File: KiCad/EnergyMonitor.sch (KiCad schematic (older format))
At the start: 28 parts

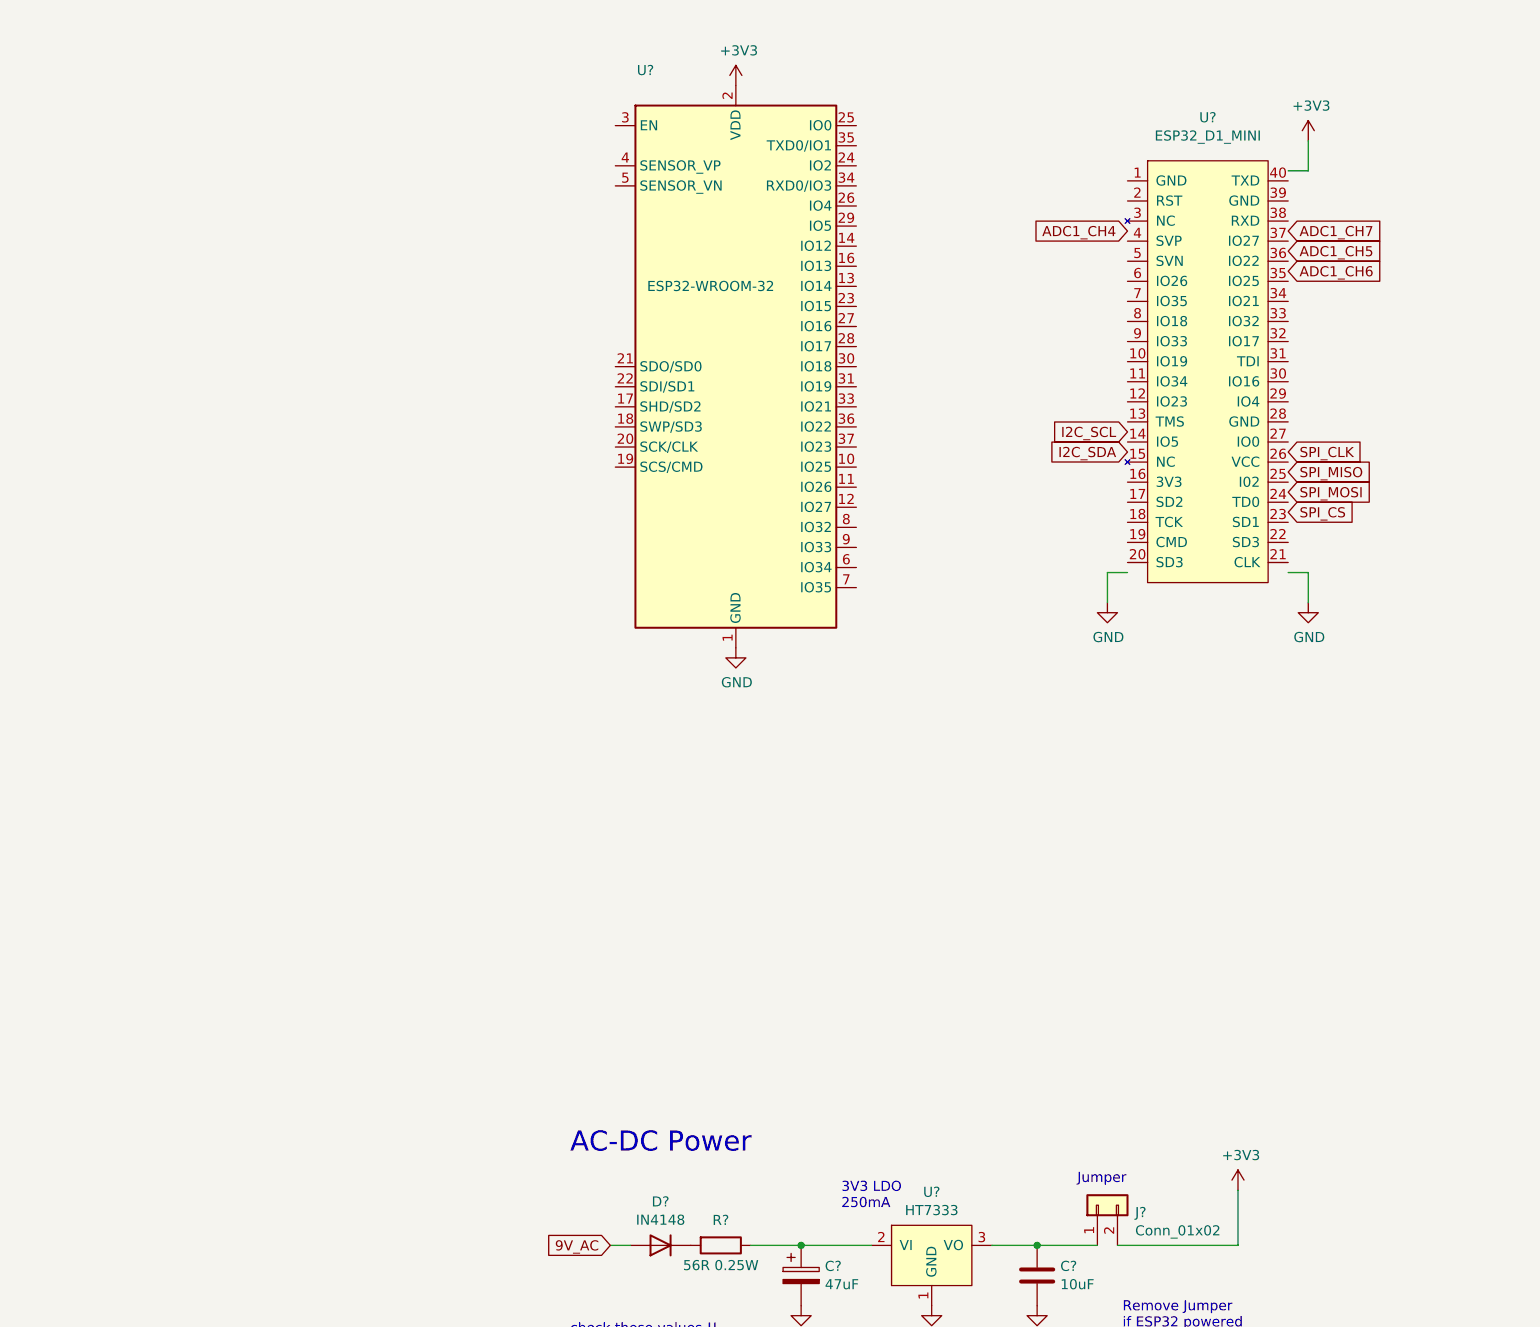
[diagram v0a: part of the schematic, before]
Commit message: edit ESP32_D1_MINI Symbol
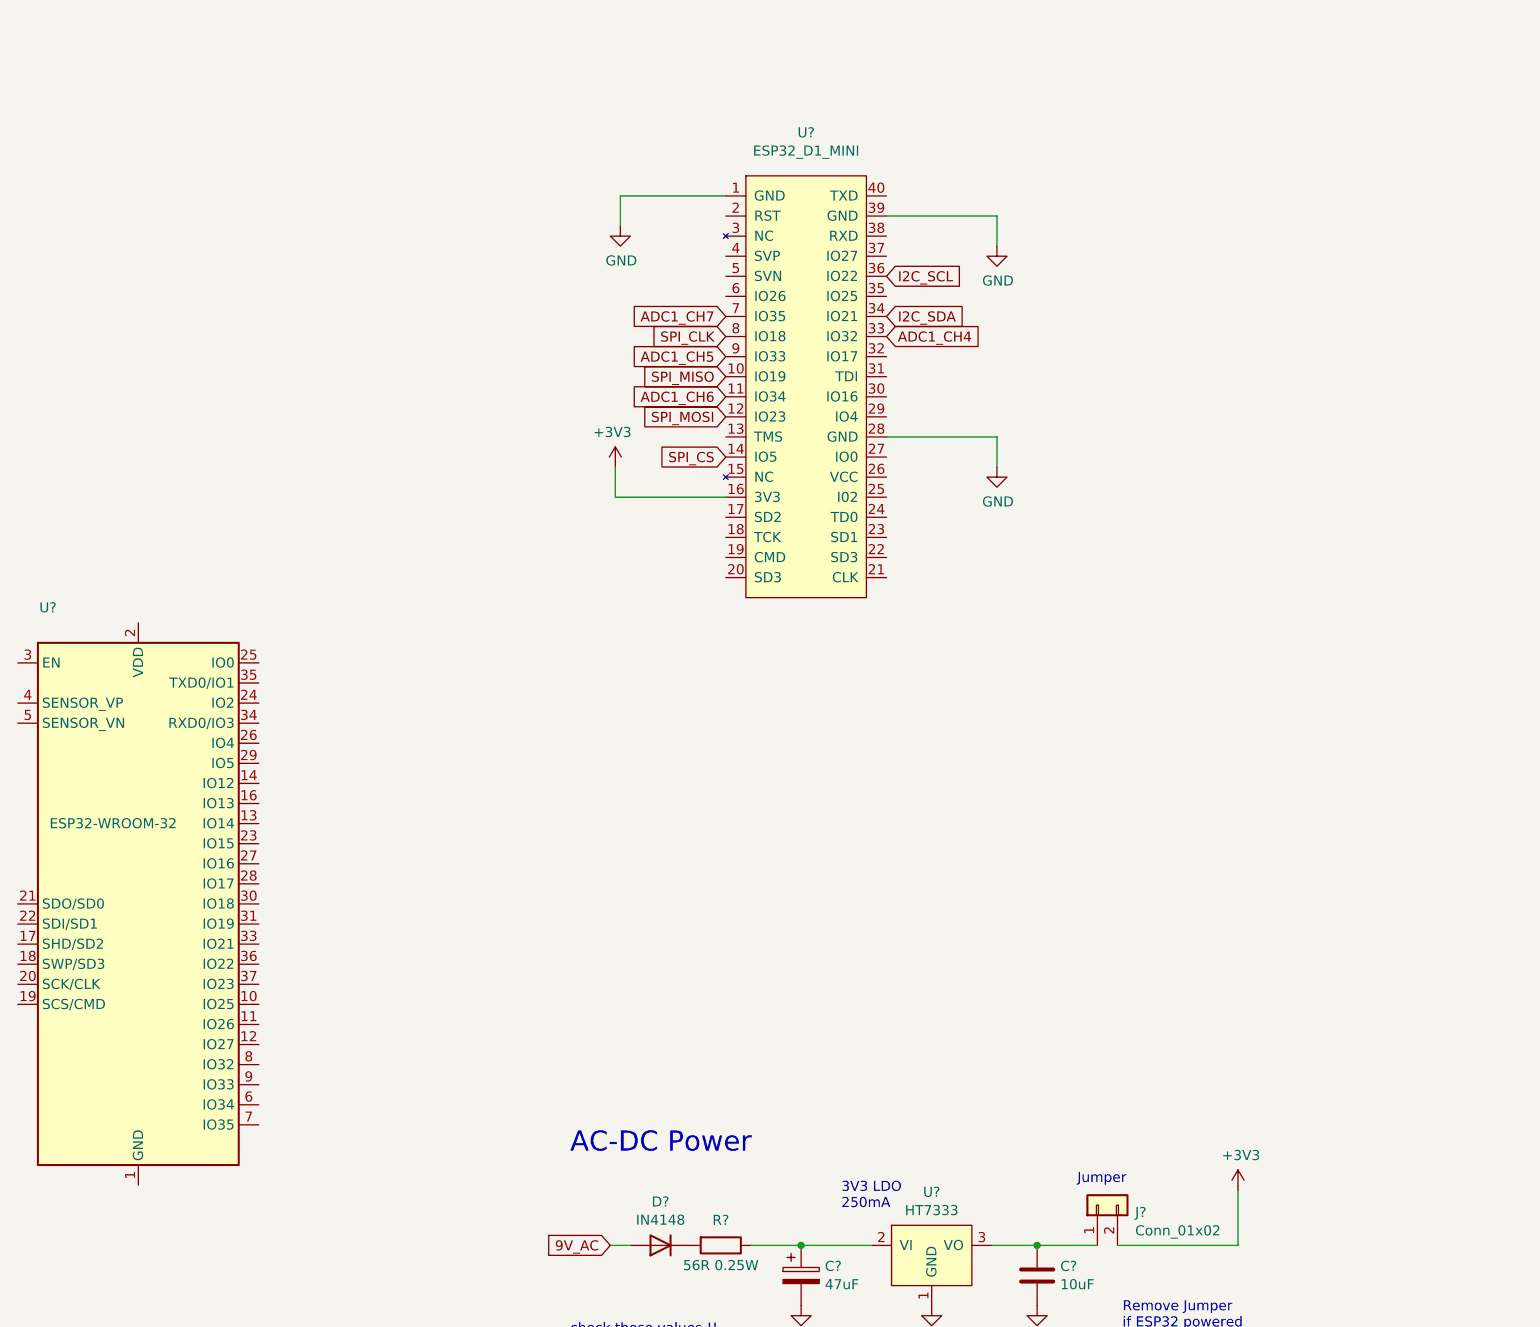
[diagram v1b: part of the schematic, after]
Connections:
- wire segments 52 -> 54
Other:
- moved on the sheet: U?
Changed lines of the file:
@@
 Sheet 1 1
 Title "ESP32 Energy Monitor"
-Date "2021-09-04"
+Date "2021-09-05"
 Rev "v1.0"
 Comp ""
@@
 Comment4 "klomar"
 $EndDescr
-Text GLabel 4450 2100 2    50   Input ~ 0
+Text GLabel 1650 2725 0    50   Input ~ 0
 ADC1_CH6
-Text GLabel 4450 1900 2    50   Input ~ 0
+Text GLabel 1650 2325 0    50   Input ~ 0
 ADC1_CH7
 $Comp
 L power:GND #PWR?
-U 1 1 6131BED5
-P 1700 3975
-F 0 "#PWR?" H 1700 3725 50  0001 C CNN
-F 1 "GND" H 1705 3802 50  0000 C CNN
-F 2 "" H 1700 3975 50  0001 C CNN
-F 3 "" H 1700 3975 50  0001 C CNN
-	1    1700 3975
-	1    0    0    -1
-$EndComp
-$Comp
-L power:+3V3 #PWR?
-U 1 1 6131CC87
-P 1700 1175
-F 0 "#PWR?" H 1700 1025 50  0001 C CNN
-F 1 "+3V3" H 1715 1348 50  0000 C CNN
-F 2 "" H 1700 1175 50  0001 C CNN
-F 3 "" H 1700 1175 50  0001 C CNN
-	1    1700 1175
-	1    0    0    -1
-$EndComp
-$Comp
-L power:GND #PWR?
 U 1 1 6135620D
 P 10225 3050
@@
 L RF_Module:ESP32-WROOM-32 U?
 U 1 1 613185A1
-P 1700 2575
-F 0 "U?" H 1250 4050 50  0000 C CNN
-F 1 "ESP32-WROOM-32" H 1575 2975 50  0000 C CNN
-F 2 "RF_Module:ESP32-WROOM-32" H 1700 1075 50  0001 C CNN
-F 3 "https://www.espressif.com/sites/default/files/documentation/esp32-wroom-32_datasheet_en.pdf" H 1400 2625 50  0001 C CNN
-	1    1700 2575
+P -1275 5250
+F 0 "U?" H -1725 6725 50  0000 C CNN
+F 1 "ESP32-WROOM-32" H -1400 5650 50  0000 C CNN
+F 2 "RF_Module:ESP32-WROOM-32" H -1275 3750 50  0001 C CNN
+F 3 "https://www.espressif.com/sites/default/files/documentation/esp32-wroom-32_datasheet_en.pdf" H -1575 5300 50  0001 C CNN
+	1    -1275 5250
 	1    0    0    -1
 $EndComp
@@
 Text Notes 3625 7450 0    50   ~ 0
 Remove Jumper\nif ESP32 powered\nby USB.
-Text GLabel 4450 2000 2    50   Input ~ 0
+Text GLabel 1650 2525 0    50   Input ~ 0
 ADC1_CH5
-Text GLabel 3650 1900 0    50   Input ~ 0
+Text GLabel 2450 2425 2    50   Input ~ 0
 ADC1_CH4
-Text GLabel 3650 2900 0    50   Input ~ 0
+Text GLabel 2450 2125 2    50   Input ~ 0
 I2C_SCL
-Text GLabel 3650 3000 0    50   Input ~ 0
+Text GLabel 2450 2325 2    50   Input ~ 0
 I2C_SDA
-Text GLabel 4450 3200 2    50   Input ~ 0
+Text GLabel 1650 2825 0    50   Input ~ 0
 SPI_MOSI
-Text GLabel 4450 3100 2    50   Input ~ 0
+Text GLabel 1650 2625 0    50   Input ~ 0
 SPI_MISO
-Text GLabel 4450 3000 2    50   Input ~ 0
+Text GLabel 1650 2425 0    50   Input ~ 0
 SPI_CLK
-Text GLabel 4450 3300 2    50   Input ~ 0
+Text GLabel 1650 3025 0    50   Input ~ 0
 SPI_CS
 Text GLabel 10475 1100 2    50   Input ~ 0
@@
 L MyComponents:ESP32_D1_MINI U?
 U 1 1 6133B216
-P 4050 2600
-F 0 "U?" H 4050 3865 50  0000 C CNN
-F 1 "ESP32_D1_MINI" H 4050 3774 50  0000 C CNN
-F 2 "" H 4050 3050 50  0001 C CNN
-F 3 "" H 4050 3050 50  0001 C CNN
-	1    4050 2600
+P 2050 2675
+F 0 "U?" H 2050 3940 50  0000 C CNN
+F 1 "ESP32_D1_MINI" H 2050 3849 50  0000 C CNN
+F 2 "" H 2050 3125 50  0001 C CNN
+F 3 "" H 2050 3125 50  0001 C CNN
+	1    2050 2675
 	1    0    0    -1
 $EndComp
@@
 L power:GND #PWR?
 U 1 1 613461CB
-P 3550 3750
-F 0 "#PWR?" H 3550 3500 50  0001 C CNN
-F 1 "GND" H 3555 3577 50  0000 C CNN
-F 2 "" H 3550 3750 50  0001 C CNN
-F 3 "" H 3550 3750 50  0001 C CNN
-	1    3550 3750
+P 1125 1875
+F 0 "#PWR?" H 1125 1625 50  0001 C CNN
+F 1 "GND" H 1130 1702 50  0000 C CNN
+F 2 "" H 1125 1875 50  0001 C CNN
+F 3 "" H 1125 1875 50  0001 C CNN
+	1    1125 1875
 	1    0    0    -1
 $EndComp
@@
 L power:GND #PWR?
 U 1 1 61346C95
-P 4550 3750
-F 0 "#PWR?" H 4550 3500 50  0001 C CNN
-F 1 "GND" H 4555 3577 50  0000 C CNN
-F 2 "" H 4550 3750 50  0001 C CNN
-F 3 "" H 4550 3750 50  0001 C CNN
-	1    4550 3750
+P 3000 1975
+F 0 "#PWR?" H 3000 1725 50  0001 C CNN
+F 1 "GND" H 3005 1802 50  0000 C CNN
+F 2 "" H 3000 1975 50  0001 C CNN
+F 3 "" H 3000 1975 50  0001 C CNN
+	1    3000 1975
 	1    0    0    -1
 $EndComp
 Wire Wire Line
-	4450 3600 4550 3600
+	2450 1825 3000 1825
 Wire Wire Line
-	4550 3600 4550 3750
+	3000 1825 3000 1975
 Wire Wire Line
-	3650 3600 3550 3600
+	1650 1725 1125 1725
 Wire Wire Line
-	3550 3600 3550 3750
+	1125 1725 1125 1875
 $Comp
 L power:+3V3 #PWR?
 U 1 1 6134B5B4
-P 4550 1450
-F 0 "#PWR?" H 4550 1300 50  0001 C CNN
-F 1 "+3V3" H 4565 1623 50  0000 C CNN
-F 2 "" H 4550 1450 50  0001 C CNN
-F 3 "" H 4550 1450 50  0001 C CNN
-	1    4550 1450
+P 1100 3075
+F 0 "#PWR?" H 1100 2925 50  0001 C CNN
+F 1 "+3V3" H 1115 3248 50  0000 C CNN
+F 2 "" H 1100 3075 50  0001 C CNN
+F 3 "" H 1100 3075 50  0001 C CNN
+	1    1100 3075
+	-1   0    0    -1
+$EndComp
+Wire Wire Line
+	1100 3075 1100 3225
+Wire Wire Line
+	1100 3225 1650 3225
+$Comp
+L power:GND #PWR?
+U 1 1 6136B822
+P 3000 3075
+F 0 "#PWR?" H 3000 2825 50  0001 C CNN
+F 1 "GND" H 3005 2902 50  0000 C CNN
+F 2 "" H 3000 3075 50  0001 C CNN
+F 3 "" H 3000 3075 50  0001 C CNN
+	1    3000 3075
 	1    0    0    -1
 $EndComp
 Wire Wire Line
-	4550 1450 4550 1600
+	2450 2925 3000 2925
 Wire Wire Line
-	4550 1600 4450 1600
+	3000 2925 3000 3075
 $EndSCHEMATC

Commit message: Circuit design - schematic
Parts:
- removed R? (x2): 120R, symbol Device:R
- added C? (x3): 10uF, symbol Device:C
- added C? (x3): 0.1uF, symbol Device:C
- added D? (x3): ESD5Z3.3T1G, symbol Device:D
- added J?: Conn_01x04, symbol Connector_Generic:Conn_01x04
- added J?: 4P4C, symbol Connector:4P4C
- added J? (x3): AudioJack3_Ground_SwitchTR, symbol Connector:AudioJack3_Ground_SwitchTR
- added J? (x3): Conn_01x02, symbol Connector_Generic:Conn_01x02
- added R? (x6): 22R, symbol Device:R
- added R? (x6): 470K, symbol Device:R
- added R? (x3): 1K, symbol Device:R
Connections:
- net labels added: ADC1_CH65
- wire segments 54 -> 125
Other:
- note added: "Burden resistance\n11R - 23kW Max @ 240V\n60R - 4kW Max @ 240V"
- note added: "I2C"
- note removed: "4kW Max @ 240V"
- note removed: "YHDC SCT-013-00 CT"
- moved on the sheet: C?, D?, J?, R?

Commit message: Cicruit design - schematic
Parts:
- removed C?: 10uF, symbol Device:C
- removed C?: 0.1uF, symbol Device:C
- removed D?: ESD5Z3.3T1G, symbol Device:D
- removed J?: AudioJack3_Ground_SwitchTR, symbol Connector:AudioJack3_Ground_SwitchTR
- removed R? (x2): 22R, symbol Device:R
- removed R? (x2): 470K, symbol Device:R
- removed R?: 1K, symbol Device:R
- removed U?: ESP32-WROOM-32, RF_Module:ESP32-WROOM-32, symbol RF_Module:ESP32-WROOM-32
- C1: renamed from C?; footprint (none) -> Capacitor_SMD:CP_Elec_5x4.4
- C10, C2, C6, C7, C8: renamed from C?; footprint (none) -> Capacitor_SMD:C_1206_3216Metric
- C3, C4, C5, C9: renamed from C?; footprint (none) -> Capacitor_SMD:C_0805_2012Metric
- D2, D3, D4, D5: renamed from D?; footprint (none) -> Diode_SMD:D_SOD-523
- J1, J5, J6, J7: renamed from J?; footprint (none) -> Connector_PinHeader_2.54mm:PinHeader_1x02_P2.54mm_Vertical
- J10: renamed from J?; footprint (none) -> MyFootprints:RJ6_4P4C_small_I2C
- J9: renamed from J?; footprint (none) -> Connector_PinHeader_2.54mm:PinHeader_1x04_P2.54mm_Vertical
- R10, R11, R12, R13, R14, R15, R16, R17, R18, R19, R2, R20, R21, R3, R4, R5, R6, R7, R8, R9: renamed from R?; footprint (none) -> Resistor_SMD:R_0805_2012Metric
- gave numbers to parts that had none: 8
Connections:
- net ADC1_CH65 is gone; now on net ADC1_CH5: D2.1 (K), R8.1
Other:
- note removed: "23kW Max @ 240V"
- moved on the sheet: C10, C9, D5, J8, R17, R18, R19, R20, R21

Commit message: pcb footprints
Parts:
- J2, J3, J4: footprint (none) -> MyFootprints:3.5mm_5_Pin_Socket_PCB_Mount
- J8: footprint (none) -> MyFootprints:DC_Barrel_Jack_Socket
- U2: footprint (none) -> MyFootprints:ESP32_D1_MINI
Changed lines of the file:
@@
 Sheet 1 1
 Title "ESP32 Energy Monitor"
-Date "2021-09-06"
+Date "2021-09-07"
 Rev "v1.0"
 Comp ""
@@
 F 0 "J8" H 7932 2517 50  0000 C CNN
 F 1 "Barrel_Jack_Switch" H 7932 2426 50  0000 C CNN
-F 2 "" H 7925 2160 50  0001 C CNN
+F 2 "MyFootprints:DC_Barrel_Jack_Socket" H 7925 2160 50  0001 C CNN
 F 3 "~" H 7925 2160 50  0001 C CNN
 	1    7875 2200
@@
 F 0 "U2" H 2050 3800 50  0000 C CNN
 F 1 "ESP32_D1_MINI" H 2050 4000 100 0000 C CNN
-F 2 "" H 2050 3125 50  0001 C CNN
+F 2 "MyFootprints:ESP32_D1_MINI" H 2050 3125 50  0001 C CNN
 F 3 "" H 2050 3125 50  0001 C CNN
 	1    2050 2675
@@
 F 0 "J2" H 4232 2325 50  0000 C CNN
 F 1 "AudioJack3_Ground_SwitchTR" H 4232 2234 50  0000 C CNN
-F 2 "" H 4250 2000 50  0001 C CNN
+F 2 "MyFootprints:3.5mm_5_Pin_Socket_PCB_Mount" H 4250 2000 50  0001 C CNN
 F 3 "~" H 4250 2000 50  0001 C CNN
 	1    4250 2000
@@
 F 0 "J3" H 4232 3775 50  0000 C CNN
 F 1 "AudioJack3_Ground_SwitchTR" H 4232 3684 50  0000 C CNN
-F 2 "" H 4250 3450 50  0001 C CNN
+F 2 "MyFootprints:3.5mm_5_Pin_Socket_PCB_Mount" H 4250 3450 50  0001 C CNN
 F 3 "~" H 4250 3450 50  0001 C CNN
 	1    4250 3450
@@
 F 0 "J4" H 4232 5225 50  0000 C CNN
 F 1 "AudioJack3_Ground_SwitchTR" H 4232 5134 50  0000 C CNN
-F 2 "" H 4250 4900 50  0001 C CNN
+F 2 "MyFootprints:3.5mm_5_Pin_Socket_PCB_Mount" H 4250 4900 50  0001 C CNN
 F 3 "~" H 4250 4900 50  0001 C CNN
 	1    4250 4900
@@
 	5650 4450 5650 4500
 Connection ~ 6500 4450
-Text Notes 8900 3350 0    100  ~ 0
+Text Notes 8925 2950 0    100  ~ 0
 I2C
 $EndSCHEMATC

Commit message: circuit design & pcb layout
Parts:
- removed J2, J3, J4: AudioJack3_Ground_SwitchTR, MyFootprints:3.5mm_5_Pin_Socket_PCB_Mount, symbol Connector:AudioJack3_Ground_SwitchTR
- removed J5, J6, J7: Conn_01x02, Connector_PinHeader_2.54mm:PinHeader_1x02_P2.54mm_Vertical, symbol Connector_Generic:Conn_01x02
- added J1, J2, J3, J4, J5, J6: Conn_01x04, Connector_PinHeader_2.54mm:PinHeader_1x04_P2.54mm_Vertical, symbol Connector_Generic:Conn_01x04
- added J10, J8, J9: AudioJack3_Ground_Switch_5_pin, MyFootprints:3.5mm_5_Pin_Socket_PCB_Mount, symbol MyComponents:AudioJack3_Ground_Switch_5_pin
- added J14: Conn_01x04, Connector_JST:JST_SH_SM04B-SRSS-TB_1x04-1MP_P1.00mm_Horizontal, symbol Connector_Generic:Conn_01x04
- added R10: 22R, Resistor_SMD:R_1206_3216Metric, symbol Device:R
- added R11: 39R, Resistor_SMD:R_1206_3216Metric, symbol Device:R
- added R12, R8: 62R, Resistor_SMD:R_1206_3216Metric, symbol Device:R
- added R13, R9: 120R, Resistor_SMD:R_1206_3216Metric, symbol Device:R
- D1: footprint (none) -> Diode_THT:D_DO-35_SOD27_P7.62mm_Horizontal
- J16: renamed from J10; footprint MyFootprints:RJ6_4P4C_small_I2C -> MyFootprints:RJ6_4P4C_small_I2C_UM10204
- R1: footprint (none) -> Resistor_SMD:R_1206_3216Metric
- R2, R6: footprint Resistor_SMD:R_0805_2012Metric -> Resistor_SMD:R_1206_3216Metric
- R3, R7: value 22R -> 39R; footprint Resistor_SMD:R_0805_2012Metric -> Resistor_SMD:R_1206_3216Metric
- R4: value 22R -> 62R; footprint Resistor_SMD:R_0805_2012Metric -> Resistor_SMD:R_1206_3216Metric
- R5: value 22R -> 120R; footprint Resistor_SMD:R_0805_2012Metric -> Resistor_SMD:R_1206_3216Metric
- renumbered J8 to J13, J9 to J15, J1 to J7, R8 to R16, R9 to R17, R10 to R18, R11 to R19, R12 to R20, R13 to R21, R14 to R22, R15 to R23, R16 to R24, R17 to R25, R18 to R26, R19 to R27, R20 to R28, R21 to R29, U2 to U1, U3 to U2
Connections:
- net +3V3: now also J14.1 (Pin_1)
- net GND: now also J14.4 (Pin_4)
- net GNDA: now also J10.S, J10.TN, J8.S, J8.TN, J9.S, J9.TN
- net I2C_SCL: now also J14.2 (Pin_2)
- net I2C_SDA: now also J14.3 (Pin_3)
- net TB1: now reaches R2.1, R5.1
- net TB1: now also C3.2, C6.1, R19.2, R20.1, R3.1, R4.1, J9.T
- net RB1: now reaches C3.1, R16.2
- net RB1: now also J1.1 (Pin_1), J1.2 (Pin_2), J1.3 (Pin_3), J1.4 (Pin_4), J9.R
- net TB2: now reaches R6.1
- net TB2: now also C4.2, C7.1, R21.2, R22.1, R7.1, J8.T, R8.1, R9.1; no longer R3.1
- net RB2: now reaches C4.1, R17.2
- net RB2: now also J2.1 (Pin_1), J2.2 (Pin_2), J2.3 (Pin_3), J2.4 (Pin_4), J8.R
- net TB3: now reaches C5.2, C8.1, R23.2, R24.1
- net TB3: now also J10.T, R10.1, R11.1, R12.1, R13.1; no longer R4.2, R7.2
- net RB3: now reaches C5.1, R18.2
- net RB3: now also J10.R, J3.1 (Pin_1), J3.2 (Pin_2), J3.3 (Pin_3), J3.4 (Pin_4)
- new net: J4.1 (Pin_1), R5.2
- new net: J4.2 (Pin_2), R4.2
- new net: J4.3 (Pin_3), R3.2
- new net: J4.4 (Pin_4), R2.2
- new net: J5.1 (Pin_1), R9.2
- new net: J5.2 (Pin_2), R8.2
- new net: J5.3 (Pin_3), R7.2
- new net: J5.4 (Pin_4), R6.2
- new net: J6.1 (Pin_1), R13.2
- new net: J6.2 (Pin_2), R12.2
- new net: J6.3 (Pin_3), R11.2
- new net: J6.4 (Pin_4), R10.2
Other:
- note added: "Check Wemos I2C pinout !"
- note added: "Should RN be connected to ground?"
- note added: "UM10204 I2C wiring"
- note added: "Wemos I2C wiring"
- note added: "a switched jack is utilized to provide a clear indication if\na CT is connected or not. When a 3.5mm plug is NOT \ninserted pin 4 is connected to pin 5 which is connected\nto GND so when no CT is connected, the ADC will sense 0V.\n\nWhen a 3.5mm plug is inserted, the connection between \npins 4 & 5 is broken and the CT channel will operate \nnormally."
- note added: "burden resistors"
- note added: "https://wiki.openenergymonitor.org/index.php/EmonTx_V3#Burden_Resistor_Calculations"
- note added: "https://www.nxp.com/docs/en/user-guide/UM10204.pdf"
- note removed: "Burden"

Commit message: circuit design & pcb layout
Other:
- note added: "trace width for burden circuits"
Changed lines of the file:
@@
 Text Notes 9325 2950 0    50   ~ 0
 UM10204 I2C wiring
-Text Notes 7400 5450 0    100  ~ 0
+Text Notes -2325 5925 0    100  ~ 0
 Check Wemos I2C pinout !
 $Comp
@@
 	1    0    0    -1
 $EndComp
-Text Notes 3500 4325 0    100  ~ 0
+Text Notes -3025 6300 0    100  ~ 0
 Should RN  be connected to ground?
 $Comp
@@
 	1    0    0    -1
 $EndComp
+Text Notes -2575 6650 0    100  ~ 0
+trace width for burden circuits
 $EndSCHEMATC

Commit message: circuit design & pcb layout
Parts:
- added D6: LED, LED_SMD:LED_0805_2012Metric, symbol Device:LED
- added H1, H2, H3, H4: MountingHole, MountingHole:MountingHole_2.2mm_M2_Pad_Via, symbol Mechanical:MountingHole
- added J11: Conn_01x02, Connector_PinHeader_2.54mm:PinHeader_1x02_P2.54mm_Vertical, symbol Connector_Generic:Conn_01x02
- added R14: 4K7, LED_SMD:LED_0805_2012Metric, symbol Device:R
- added TP1, TP2, TP3, TP4, TP5: TestPoint_Probe, TestPoint:TestPoint_Loop_D2.50mm_Drill1.0mm_LowProfile, symbol Connector:TestPoint_Probe
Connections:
- net +3V3: now also R14.1
- net 9V_AC: now also J11.1 (Pin_1); no longer D1.2 (A)
- net ADC1_CH4: now also TP4.1
- net ADC1_CH5: now also TP1.1
- net ADC1_CH6: now also TP2.1
- net ADC1_CH7: now also TP3.1
- net GND: now also D6.1 (K), TP5.1
- new net: D1.2 (A), J11.2 (Pin_2)
- new net: D6.2 (A), R14.2
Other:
- note added: "red superbright LED\n0805 SMD\ngreen band -ve\n1k R => 1.4mA\n4K7 => 0.3mA\n@3.3v"
- moved on the sheet: C1, C2, D1, J7, R1, U2
